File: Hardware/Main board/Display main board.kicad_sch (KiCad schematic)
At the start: 1 part, among them J1 Board to Board

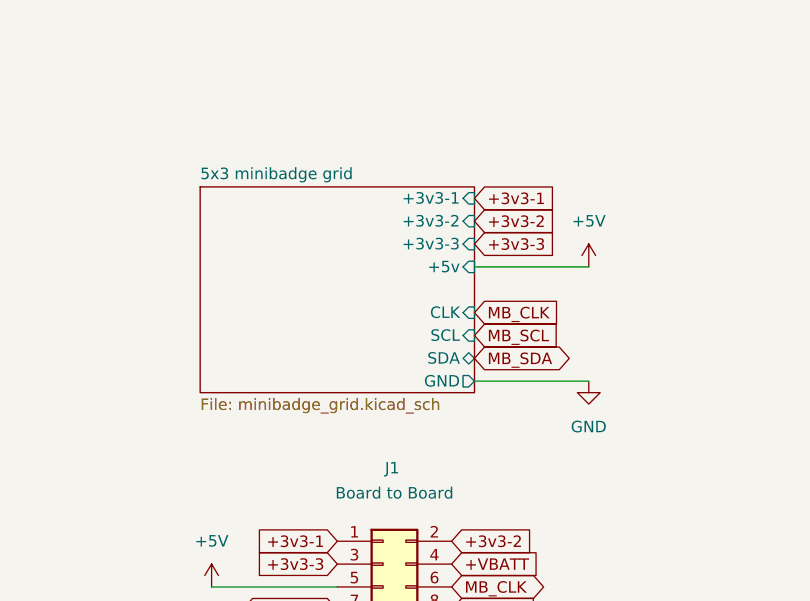
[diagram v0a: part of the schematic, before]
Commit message: Big changes
- Folder changes
- change dimensions of board to match thicker material
- begin part selection/footprint selection
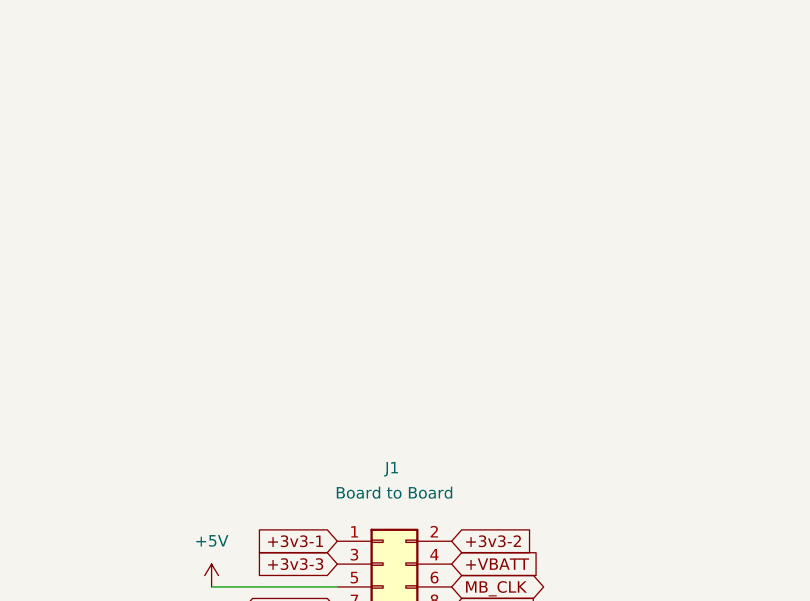
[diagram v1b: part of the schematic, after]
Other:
- removed sheet 5x3 minibadge grid

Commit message: Schematic changes
- changed positions/schematic values and nets
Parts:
- J1: footprint (none) -> Connector_PinSocket_2.54mm:PinSocket_2x05_P2.54mm_Vertical_SMD
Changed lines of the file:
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@@
 			)
 		)
-		(property "Footprint" ""
+		(property "Footprint" "Connector_PinSocket_2.54mm:PinSocket_2x05_P2.54mm_Vertical_SMD"
 			(at 198.12 142.24 0)
 			(effects

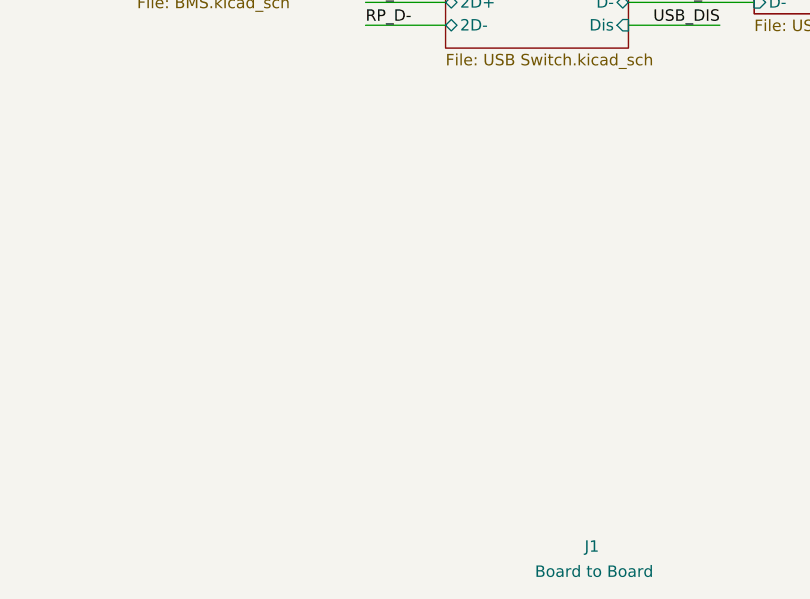
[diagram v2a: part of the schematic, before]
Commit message: FIxing issues
- Messed up mounting holes
- board didn't copy to front plate
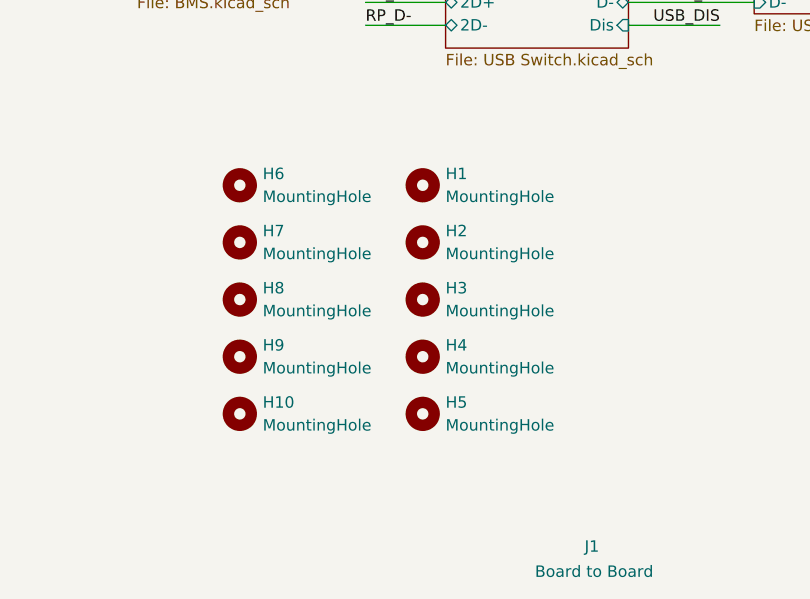
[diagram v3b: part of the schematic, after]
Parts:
- added H1, H10, H2, H3, H4, H5, H6, H7, H8, H9: MountingHole, symbol Mechanical:MountingHole

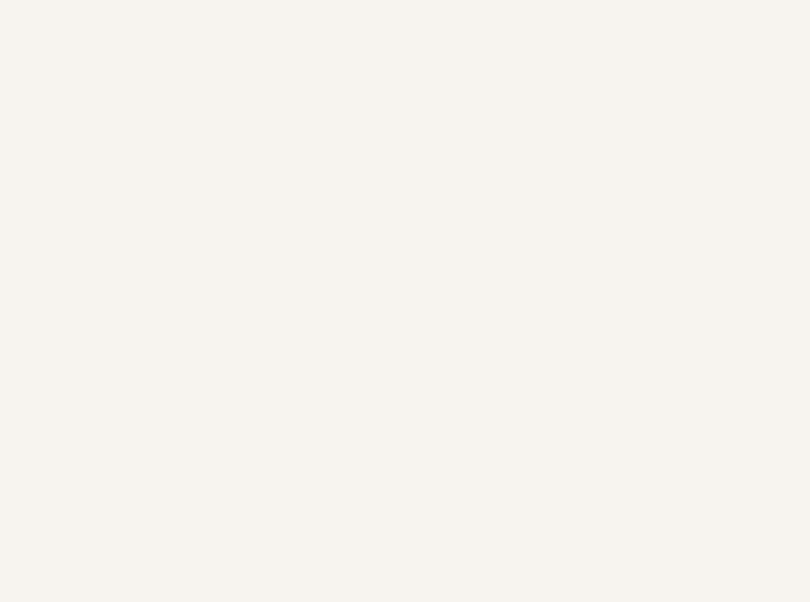
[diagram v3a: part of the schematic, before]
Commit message: Add Voltage Regulators
TLV1117LV33
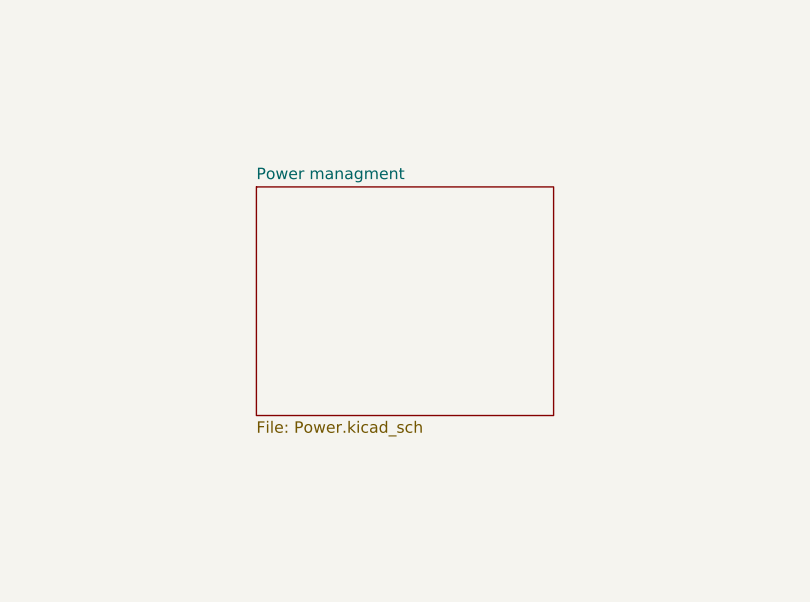
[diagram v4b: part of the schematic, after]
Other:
- added sheet Power managment (Power.kicad_sch)
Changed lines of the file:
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@@
+	)
+	(sheet
+		(at 67.31 68.58)
+		(size 33.02 25.4)
+		(fields_autoplaced yes)
+		(stroke
+			(width 0.1524)
+			(type solid)
+		)
+		(fill
+			(color 0 0 0 0.0000)
+		)
+		(property "Sheetname" "Power managment"
+			(at 67.31 67.8684 0)
+			(effects
+				(font
+					(size 1.27 1.27)
+				)
+				(justify left bottom)
+			)
+		)
+		(property "Sheetfile" "Power.kicad_sch"
+			(at 67.31 94.5646 0)
+			(effects
+				(font
+					(size 1.27 1.27)
+				)
+				(justify left top)
+			)
+		)
+		(instances
+			(project "Display main board"
+				(path "/e5119d15-74fb-4259-abbc-5cab1f368532"
+					(page "7")
+				)
+			)
+		)
 	)
 	(sheet

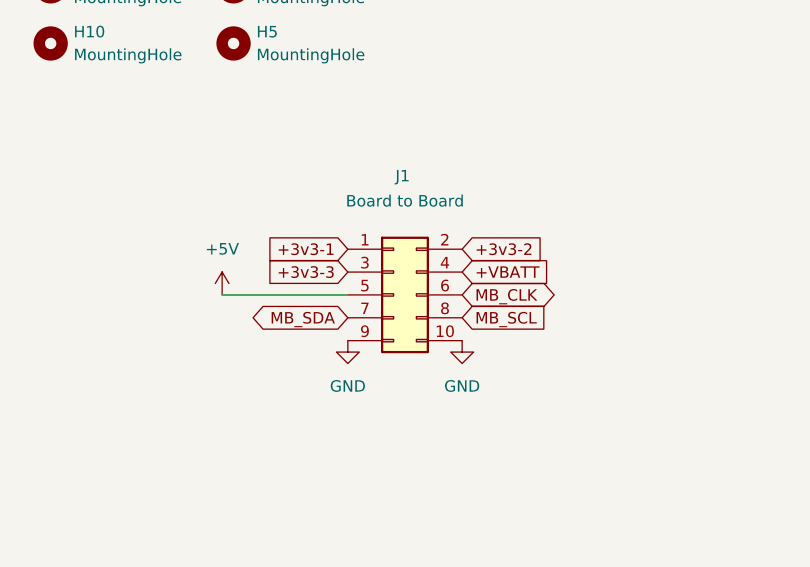
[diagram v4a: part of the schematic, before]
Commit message: hardware changes and initial traces/layout
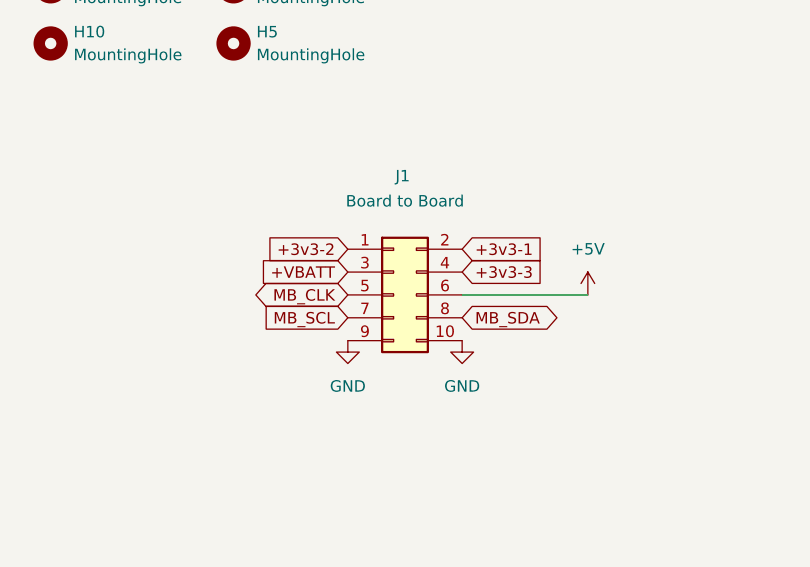
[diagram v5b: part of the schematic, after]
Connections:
- net +3v3-1: now also J1.2 (Pin_2); no longer J1.1 (Pin_1)
- net +3v3-2: now also J1.1 (Pin_1); no longer J1.2 (Pin_2)
- net +3v3-3: now also J1.4 (Pin_4); no longer J1.3 (Pin_3)
- net +5V: now also J1.6 (Pin_6); no longer J1.5 (Pin_5)
- net +VBATT: now also J1.3 (Pin_3); no longer J1.4 (Pin_4)
- net MB_CLK: now also J1.5 (Pin_5); no longer J1.6 (Pin_6)
- net MB_SCL: now also J1.7 (Pin_7); no longer J1.8 (Pin_8)
- net MB_SDA: now also J1.8 (Pin_8); no longer J1.7 (Pin_7)
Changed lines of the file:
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@@
-	(wire
-		(pts
-			(xy 179.07 142.24) (xy 193.04 142.24)
-		)
-		(stroke
-			(width 0)
-			(type default)
-		)
-	)
 	(wire
 		(pts
@@
 		(pts
 			(xy 276.86 53.34) (xy 285.75 53.34)
+		)
+		(stroke
+			(width 0)
+			(type default)
+		)
+	)
+	(wire
+		(pts
+			(xy 219.71 142.24) (xy 205.74 142.24)
 		)
 		(stroke
@@
 		)
 	)
-	(global_label "+VBATT"
+	(global_label "MB_SDA"
+		(shape bidirectional)
+		(at 205.74 144.78 0)
+		(fields_autoplaced yes)
+		(effects
+			(font
+				(size 1.27 1.27)
+			)
+			(justify left)
+		)
+		(property "Intersheetrefs" "${INTERSHEET_REFS}"
+			(at 217.0936 144.78 0)
+			(effects
+				(font
+					(size 1.27 1.27)
+				)
+				(justify left)
+				(hide yes)
+			)
+		)
+	)
+	(global_label "MB_SCL"
 		(shape input)
-		(at 205.74 139.7 0)
-		(fields_autoplaced yes)
-		(effects
-			(font
-				(size 1.27 1.27)
-			)
-			(justify left)
-		)
-		(property "Intersheetrefs" "${INTERSHEET_REFS}"
-			(at 214.1076 139.7 0)
-			(effects
-				(font
-					(size 1.27 1.27)
-				)
-				(justify left)
+		(at 193.04 144.78 180)
+		(fields_autoplaced yes)
+		(effects
+			(font
+				(size 1.27 1.27)
+			)
+			(justify right)
+		)
+		(property "Intersheetrefs" "${INTERSHEET_REFS}"
+			(at 181.7469 144.78 0)
+			(effects
+				(font
+					(size 1.27 1.27)
+				)
+				(justify right)
 				(hide yes)
 			)
@@
 		)
 	)
-	(global_label "+3v3-2"
+	(global_label "+3v3-1"
 		(shape input)
 		(at 205.74 137.16 0)
@@
 		)
 	)
-	(global_label "+3v3-1"
-		(shape input)
-		(at 193.04 137.16 180)
+	(global_label "MB_CLK"
+		(shape bidirectional)
+		(at 193.04 142.24 180)
 		(fields_autoplaced yes)
 		(effects
@@
 		)
 		(property "Intersheetrefs" "${INTERSHEET_REFS}"
-			(at 182.3139 137.16 0)
-			(effects
-				(font
-					(size 1.27 1.27)
-				)
-				(justify right)
-				(hide yes)
-			)
-		)
-	)
-	(global_label "MB_SCL"
-		(shape input)
-		(at 205.74 144.78 0)
-		(fields_autoplaced yes)
-		(effects
-			(font
-				(size 1.27 1.27)
-			)
-			(justify left)
-		)
-		(property "Intersheetrefs" "${INTERSHEET_REFS}"
-			(at 217.0331 144.78 0)
-			(effects
-				(font
-					(size 1.27 1.27)
-				)
-				(justify left)
-				(hide yes)
-			)
-		)
-	)
-	(global_label "MB_SDA"
-		(shape bidirectional)
-		(at 193.04 144.78 180)
-		(fields_autoplaced yes)
-		(effects
-			(font
-				(size 1.27 1.27)
-			)
-			(justify right)
-		)
-		(property "Intersheetrefs" "${INTERSHEET_REFS}"
-			(at 181.6864 144.78 0)
-			(effects
-				(font
-					(size 1.27 1.27)
-				)
-				(justify right)
-				(hide yes)
-			)
-		)
-	)
-	(global_label "+3v3-3"
-		(shape input)
-		(at 193.04 139.7 180)
-		(fields_autoplaced yes)
-		(effects
-			(font
-				(size 1.27 1.27)
-			)
-			(justify right)
-		)
-		(property "Intersheetrefs" "${INTERSHEET_REFS}"
-			(at 182.3139 139.7 0)
+			(at 181.6864 142.24 0)
 			(effects
 				(font
@@
 		)
 	)
+	(global_label "+VBATT"
+		(shape input)
+		(at 193.04 139.7 180)
+		(fields_autoplaced yes)
+		(effects
+			(font
+				(size 1.27 1.27)
+			)
+			(justify right)
+		)
+		(property "Intersheetrefs" "${INTERSHEET_REFS}"
+			(at 184.6724 139.7 0)
+			(effects
+				(font
+					(size 1.27 1.27)
+				)
+				(justify right)
+				(hide yes)
+			)
+		)
+	)
+	(global_label "+3v3-3"
+		(shape input)
+		(at 205.74 139.7 0)
+		(fields_autoplaced yes)
+		(effects
+			(font
+				(size 1.27 1.27)
+			)
+			(justify left)
+		)
+		(property "Intersheetrefs" "${INTERSHEET_REFS}"
+			(at 216.4661 139.7 0)
+			(effects
+				(font
+					(size 1.27 1.27)
+				)
+				(justify left)
+				(hide yes)
+			)
+		)
+	)
 	(global_label "SYS_SCL"
 		(shape output)
@@
 		)
 	)
+	(global_label "+3v3-2"
+		(shape input)
+		(at 193.04 137.16 180)
+		(fields_autoplaced yes)
+		(effects
+			(font
+				(size 1.27 1.27)
+			)
+			(justify right)
+		)
+		(property "Intersheetrefs" "${INTERSHEET_REFS}"
+			(at 182.3139 137.16 0)
+			(effects
+				(font
+					(size 1.27 1.27)
+				)
+				(justify right)
+				(hide yes)
+			)
+		)
+	)
 	(global_label "MB_SDA"
 		(shape bidirectional)
@@
 		(property "Intersheetrefs" "${INTERSHEET_REFS}"
 			(at 350.6023 55.88 0)
-			(effects
-				(font
-					(size 1.27 1.27)
-				)
-				(justify left)
-				(hide yes)
-			)
-		)
-	)
-	(global_label "MB_CLK"
-		(shape bidirectional)
-		(at 205.74 142.24 0)
-		(fields_autoplaced yes)
-		(effects
-			(font
-				(size 1.27 1.27)
-			)
-			(justify left)
-		)
-		(property "Intersheetrefs" "${INTERSHEET_REFS}"
-			(at 217.0936 142.24 0)
 			(effects
 				(font
@@
 				(path "/e5119d15-74fb-4259-abbc-5cab1f368532"
 					(reference "H10")
+					(unit 1)
+				)
+			)
+		)
+	)
+	(symbol
+		(lib_id "power:+5V")
+		(at 219.71 142.24 0)
+		(mirror y)
+		(unit 1)
+		(exclude_from_sim no)
+		(in_bom yes)
+		(on_board yes)
+		(dnp no)
+		(fields_autoplaced yes)
+		(property "Reference" "#PWR01"
+			(at 219.71 146.05 0)
+			(effects
+				(font
+					(size 1.27 1.27)
+				)
+				(hide yes)
+			)
+		)
+		(property "Value" "+5V"
+			(at 219.71 137.16 0)
+			(effects
+				(font
+					(size 1.27 1.27)
+				)
+			)
+		)
+		(property "Footprint" ""
+			(at 219.71 142.24 0)
+			(effects
+				(font
+					(size 1.27 1.27)
+				)
+				(hide yes)
+			)
+		)
+		(property "Datasheet" ""
+			(at 219.71 142.24 0)
+			(effects
+				(font
+					(size 1.27 1.27)
+				)
+				(hide yes)
+			)
+		)
+		(property "Description" "Power symbol creates a global label with name \"+5V\""
+			(at 219.71 142.24 0)
+			(effects
+				(font
+					(size 1.27 1.27)
+				)
+				(hide yes)
+			)
+		)
+		(pin "1"
+		)
+		(instances
+			(project "Display main board"
+				(path "/e5119d15-74fb-4259-abbc-5cab1f368532"
+					(reference "#PWR01")
 					(unit 1)
 				)
@@
 					(unit 1)
 				)
-			)
-		)
-	)
-	(symbol
-		(lib_id "power:+5V")
-		(at 179.07 142.24 0)
-		(unit 1)
-		(exclude_from_sim no)
-		(in_bom yes)
-		(on_board yes)
-		(dnp no)
-		(fields_autoplaced yes)
-		(property "Reference" "#PWR01"
-			(at 179.07 146.05 0)
-			(effects
-				(font
-					(size 1.27 1.27)
-				)
-				(hide yes)
-			)
-		)
-		(property "Value" "+5V"
-			(at 179.07 137.16 0)
-			(effects
-				(font
-					(size 1.27 1.27)
-				)
-			)
-		)
-		(property "Footprint" ""
-			(at 179.07 142.24 0)
-			(effects
-				(font
-					(size 1.27 1.27)
-				)
-				(hide yes)
-			)
-		)
-		(property "Datasheet" ""
-			(at 179.07 142.24 0)
-			(effects
-				(font
-					(size 1.27 1.27)
-				)
-				(hide yes)
-			)
-		)
-		(property "Description" "Power symbol creates a global label with name \"+5V\""
-			(at 179.07 142.24 0)
-			(effects
-				(font
-					(size 1.27 1.27)
-				)
-				(hide yes)
-			)
-		)
-		(pin "1"
-		)
-		(instances
-			(project "Minibadge Display 5x3"
-				(path "/e5119d15-74fb-4259-abbc-5cab1f368532"
-					(reference "#PWR01")
-					(unit 1)
-				)

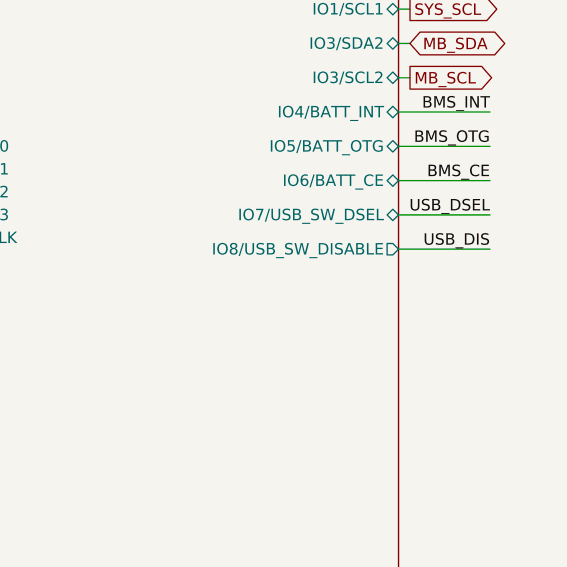
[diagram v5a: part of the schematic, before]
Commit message: update power for TPM
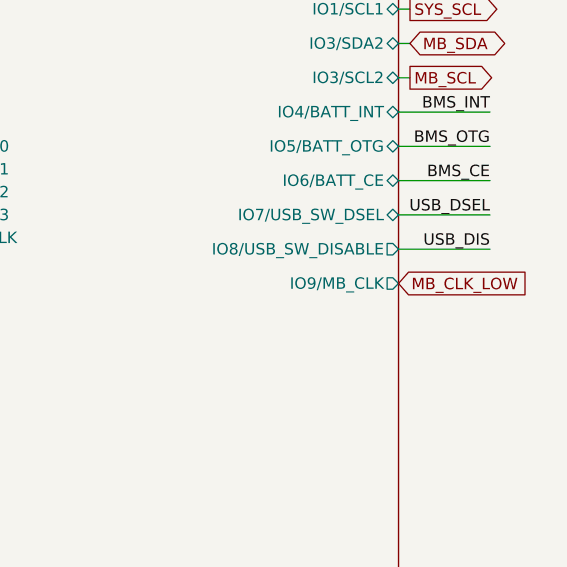
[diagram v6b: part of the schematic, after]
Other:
- sheet RP2040 ports: added IO9/MB_CLK; removed none
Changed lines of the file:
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@@
+		)
+	)
+	(global_label "MB_CLK_LOW"
+		(shape input)
+		(at 339.09 82.55 0)
+		(fields_autoplaced yes)
+		(effects
+			(font
+				(size 1.27 1.27)
+			)
+			(justify left)
+		)
+		(property "Intersheetrefs" "${INTERSHEET_REFS}"
+			(at 354.1099 82.55 0)
+			(effects
+				(font
+					(size 1.27 1.27)
+				)
+				(justify left)
+				(hide yes)
+			)
 		)
 	)
@@
 			(effects
 				(font
+					(size 1.27 1.27)
+				)
+				(justify right)
+			)
+		)
+		(pin "IO9{slash}MB_CLK" output
+			(at 339.09 82.55 0)
+			(effects
+				(font

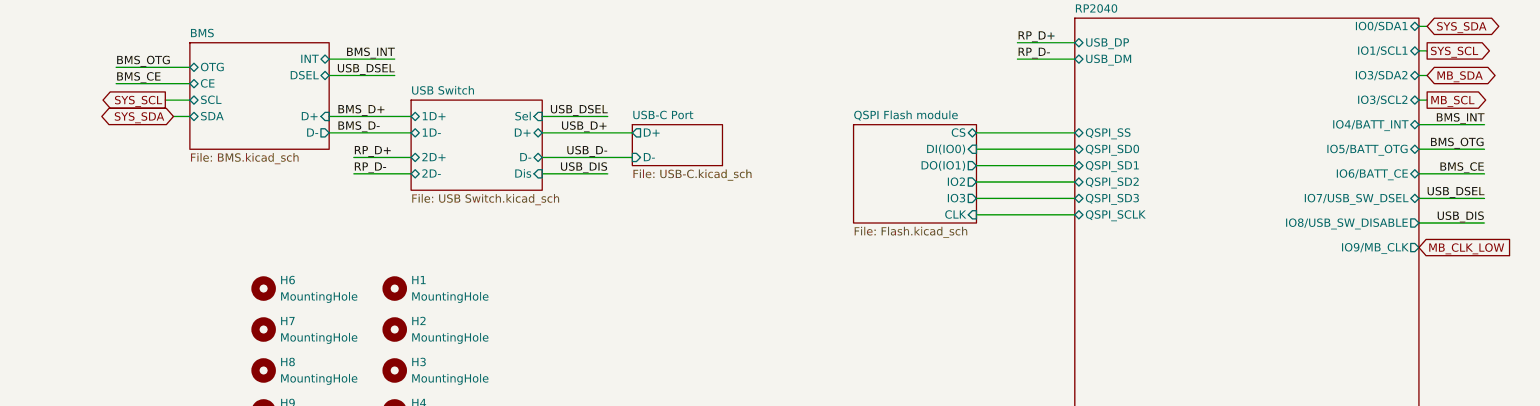
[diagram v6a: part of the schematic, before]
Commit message: Fixed BMS_STAT pin
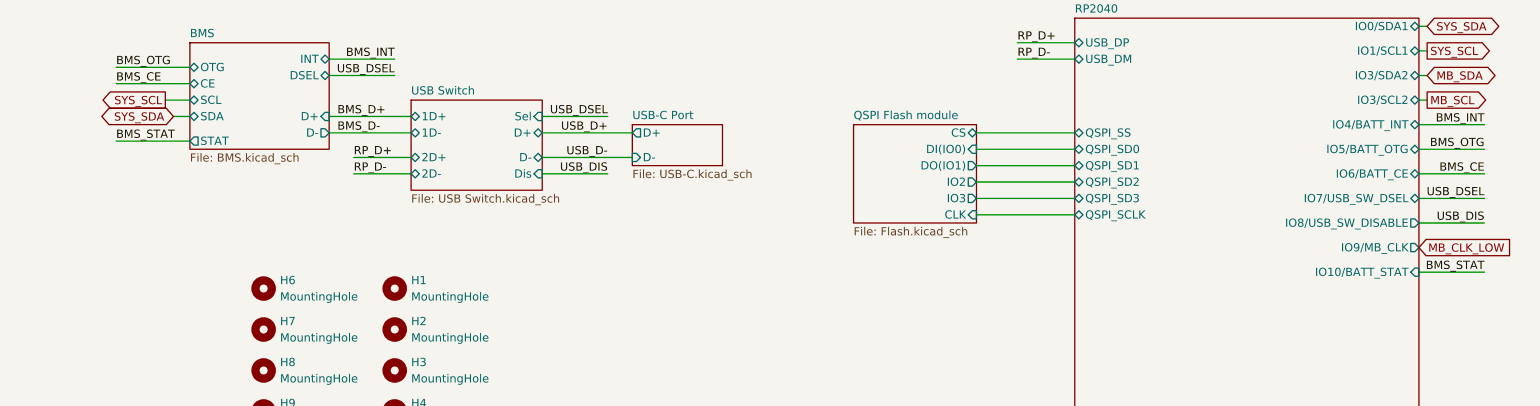
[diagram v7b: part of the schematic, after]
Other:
- sheet BMS ports: added STAT; removed none
- sheet RP2040 ports: added IO10/BATT_STAT; removed none
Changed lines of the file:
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@@
+	(wire
+		(pts
+			(xy 137.16 66.04) (xy 148.59 66.04)
+		)
+		(stroke
+			(width 0)
+			(type default)
+		)
+	)
 	(wire
 		(pts
@@
 		(pts
 			(xy 170.18 62.23) (xy 182.88 62.23)
+		)
+		(stroke
+			(width 0)
+			(type default)
+		)
+	)
+	(wire
+		(pts
+			(xy 339.09 86.36) (xy 349.25 86.36)
 		)
 		(stroke
@@
 		)
 	)
+	(label "BMS_STAT"
+		(at 137.16 66.04 0)
+		(effects
+			(font
+				(size 1.27 1.27)
+			)
+			(justify left bottom)
+		)
+	)
 	(label "USB_DIS"
 		(at 213.36 71.12 180)
@@
 	(label "USB_DSEL"
 		(at 180.34 55.88 180)
+		(effects
+			(font
+				(size 1.27 1.27)
+			)
+			(justify right bottom)
+		)
+	)
+	(label "BMS_STAT"
+		(at 349.25 86.36 180)
 		(effects
 			(font
@@
 			)
 		)
+		(pin "IO10{slash}BATT_STAT" input
+			(at 339.09 86.36 0)
+			(effects
+				(font
+					(size 1.27 1.27)
+				)
+				(justify right)
+			)
+		)
 		(instances
 			(project "Display main board"
@@
 			(effects
 				(font
+					(size 1.27 1.27)
+				)
+				(justify left)
+			)
+		)
+		(pin "STAT" output
+			(at 148.59 66.04 180)
+			(effects
+				(font
